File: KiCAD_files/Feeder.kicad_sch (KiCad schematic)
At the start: 118 parts, among them J501 Conn_01x03, Q501 60V N channel, Q502 TK13P25D,RQ, T501 PA2467NL, U501 NCP12700, U502 HMHA2801A, U503 TL431MFDT,215

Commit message: dev
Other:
- title: TWIST V1.2 -> Inverter V0.1

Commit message: correcter duplicate feeder comp
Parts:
- removed C501, C502: 470nF, Footprints:C_0805_2012Metric, symbol Device:C
- removed C503, C504, C505, C506: 4.7uF, Footprints:C_1210_3225Metric, symbol Device:C
- removed C507: 10nF, Footprints:C_0805_2012Metric, symbol Device:C
- removed C508: 22nF, Footprints:C_0805_2012Metric, symbol Device:C
- removed C509, C518: 1nF, Footprints:C_0805_2012Metric, symbol Device:C
- removed C510: C0G, 100pF, Footprints:C_0805_2012Metric, symbol Device:C
- removed C511: X7T, 100nF, Footprints:C_0805_2012Metric, symbol Device:C
- removed C512, C513: 1uF, Footprints:C_0805_2012Metric, symbol Device:C
- removed C514, C520: 6.8nF, Footprints:C_0805_2012Metric, symbol Device:C
- removed C515: 100pF, Capacitor_SMD:C_1206_3216Metric, symbol Device:C
- removed C516, C517: 2.2nF, Capacitor_SMD:C_1812_4532Metric, symbol Device:C
- removed C519: 10uF, Footprints:C_1210_3225Metric, symbol Device:C
- removed C521: 100uF, Capacitor_SMD:CP_Elec_6.3x7.7, symbol Device:C_Polarized_Small
- removed D501: 6.2V, Footprints:D_SOD-323, symbol Device:D_Zener
- removed D502, D503, D505, D506: BAS20HT1G, Footprints:D_SOD-323, symbol Device:D
- removed D504: MURA130T3G, Diode_SMD:D_SMA, symbol Device:D
- removed D507: STTH4R02U, Diode_SMD:D_SMB, symbol Device:D_Schottky
- removed J501: Conn_01x03, Connector_PinHeader_2.54mm:PinHeader_1x03_P2.54mm_Vertical, symbol Connector_Generic:Conn_01x03
- removed JP501: Jumper_2_Bridged, Jumper:SolderJumper-2_P1.3mm_Bridged2Bar_Pad1.0x1.5mm, symbol Jumper:Jumper_2_Bridged
- removed L501: 10uH, Inductor_SMD:L_1210_3225Metric, symbol Device:L
- removed L502: 100uH, Inductor_SMD:L_0805_2012Metric, symbol Device:L_Small
- removed NTC501: 100kNTC, Footprints:R_0805_2012Metric, symbol Device:Thermistor_NTC
- removed Q501: 60V N channel, Footprints:SOT-23_copy, symbol Device:Q_NMOS_GSD
- removed Q502: TK13P25D,RQ, Package_TO_SOT_SMD:TO-252-2, symbol Device:Q_NMOS_GDS
- removed R501, R509: 348k, Footprints:R_0805_2012Metric, symbol Device:R
- removed R502, R518: 27k, Footprints:R_0805_2012Metric, symbol Device:R
- removed R503: 100k, Footprints:R_0805_2012Metric, symbol Device:R
- removed R504, R512: 1.4k, Footprints:R_0805_2012Metric, symbol Device:R
- removed R505: 2.2R, Footprints:R_0805_2012Metric, symbol Device:R
- removed R506: 470R, Footprints:R_0805_2012Metric, symbol Device:R
- removed R507, R511, R516: 10R, Footprints:R_0805_2012Metric, symbol Device:R
- removed R508, R515: 10k, Footprints:R_0805_2012Metric, symbol Device:R
- removed R510: 240m, Resistor_SMD:R_1210_3225Metric, symbol Device:R
- removed R513: 10R, Resistor_SMD:R_2010_5025Metric, symbol Device:R
- removed R517: 38.3k, Footprints:R_0805_2012Metric, symbol Device:R
- removed T501: PA2467NL, Footprints:PA2467NL, symbol Symbols:PA2467NL
- removed U501: NCP12700, Package_SO:MSOP-10_3x3mm_P0.5mm, symbol Symbols:NCP12700
- renumbered C501 to C502, C502 to C503, C503 to C506, C504 to C507, C505 to C509, C506 to C510, C507 to C513, C508 to C517, C509 to C520, C510 to C522, C511 to C524, C512 to C525, C513 to C526, C514 to C529, C515 to C530, C516 to C532, C517 to C534, C518 to C536, C519 to C539, C520 to C540, C521 to C542, D503 to D504, D504 to D507, D505 to D508, D506 to D511, D507 to D512, GND501 to GND502, J501 to J502, JP501 to JP502, L502 to L504, Q501 to Q502, Q502 to Q504, R502 to R504, R503 to R505, R504 to R506, R505 to R507, R506 to R509, R507 to R511, R508 to R514, R509 to R515, R510 to R517, R511 to R519, R512 to R522, R513 to R524, R514 to R525, R514 to R526, R515 to R528, R516 to R530, R517 to R531, R518 to R533, U501 to U502, U502 to U503, U502 to U504, U503 to U505, U503 to U506, VOUT_GND501 to VOUT_GND502
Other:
- note added: "Type 2 Isolated feedback network with TL431 As per Application note DN05109-D Explanation https://www.onsemi.com/pub/Collateral/TND381-D.PDF R15 is the value to change the output voltage It should be 27K to stabilize it to 6.05V TL431 give Vo = 6.05V with Vo = Vref(1 + R14/R15) 6.05V = 2,5V * (1 + 38,3K/27K)"
- note removed: "Added inductor and extra capacitors for the input filter as per application note"
- note removed: "R15 is the value to change the output voltage It should be 27K to stabilize it to 6.05V"
- note removed: "TL431 give Vo = 6.05V with Vo = Vref(1 + R14/R15) 6.05V = 2,5V * (1 + 38,3K/27K)"
- note removed: "Type 2 Isolated feedback network with TL431 As per Application note DN05109-D Explanation https://www.onsemi.com/pub/Collateral/TND381-D.PDF"

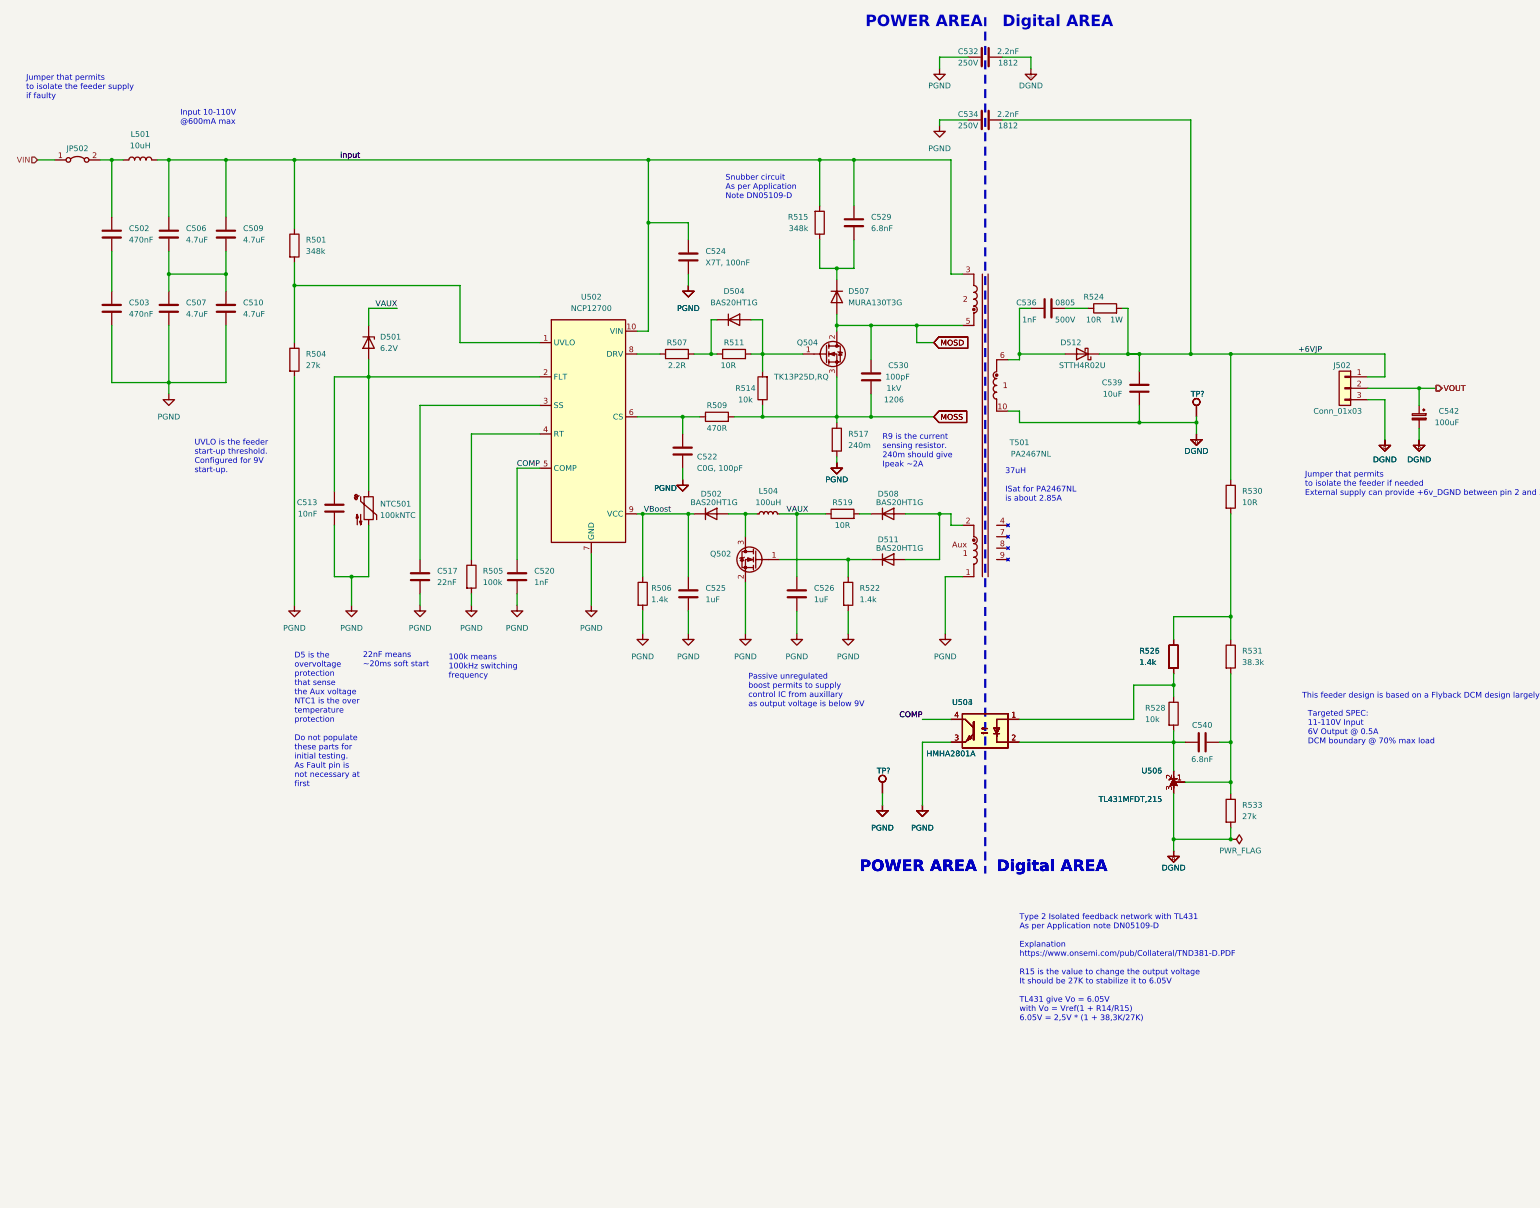
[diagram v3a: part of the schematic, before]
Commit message: reorganized with more subsheet
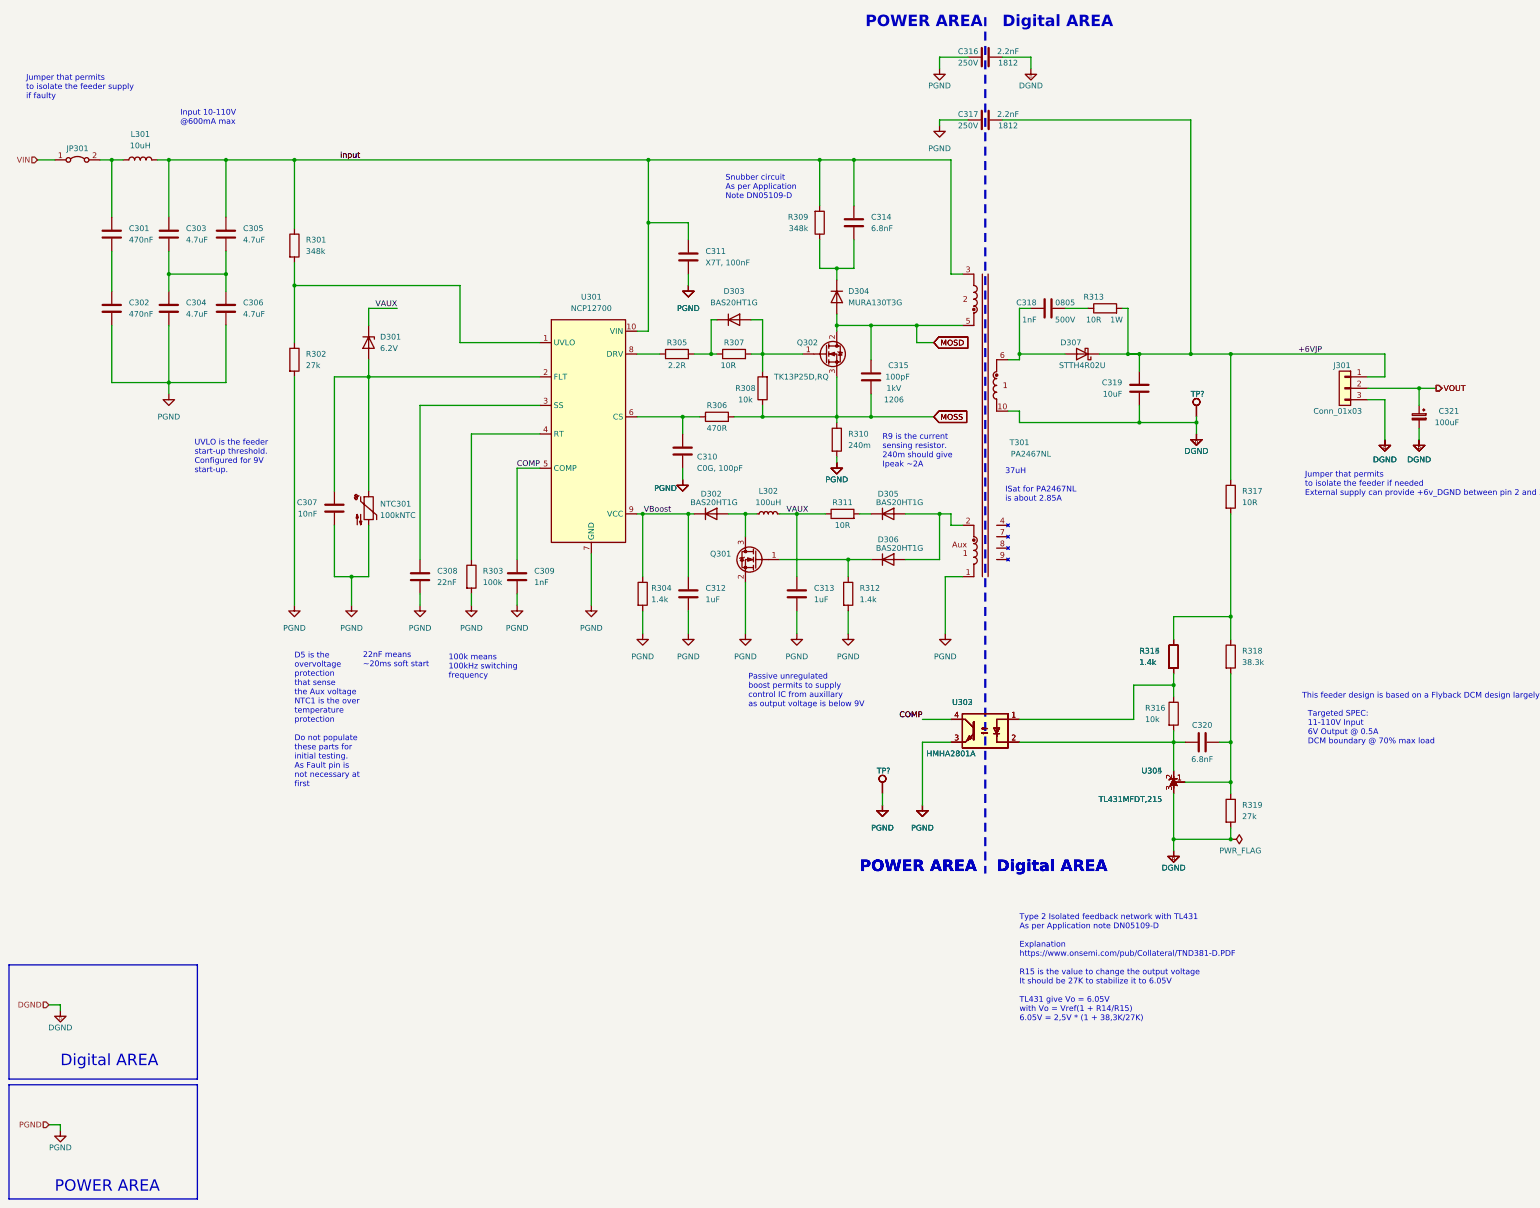
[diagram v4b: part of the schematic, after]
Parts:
- renumbered C502 to C301, C503 to C302, C506 to C303, C507 to C304, C509 to C305, C510 to C306, C513 to C307, C517 to C308, C520 to C309, C522 to C310, C524 to C311, C525 to C312, C526 to C313, C529 to C314, C530 to C315, C532 to C316, C534 to C317, C536 to C318, C539 to C319, C540 to C320, C542 to C321, D501 to D301, D502 to D302, D504 to D303, D507 to D304, D508 to D305, D511 to D306, D512 to D307, GND501 to GND301, GND502 to GND302, J502 to J301, JP502 to JP301, L501 to L301, L504 to L302, NTC501 to NTC301, Q502 to Q301, Q504 to Q302, R501 to R301, R504 to R302, R505 to R303, R506 to R304, R507 to R305, R509 to R306, R511 to R307, R514 to R308, R515 to R309, R517 to R310, R519 to R311, R522 to R312, R524 to R313, R525 to R314, R526 to R315, R528 to R316, R530 to R317, R531 to R318, R533 to R319, T501 to T301, U502 to U301, U503 to U302, U504 to U303, U505 to U304, U506 to U305, VOUT_GND501 to VOUT_GND301, VOUT_GND502 to VOUT_GND302
